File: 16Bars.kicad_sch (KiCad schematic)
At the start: 35 parts, among them IC1 CD4033BE, IC2 CD4033BE, IC3 CD4510BE, J1 CLOCK_IN, J2 Conn_02x05_Odd_Even, Q1 2N3904, Q2 2N3904, Q3 2N3904, Q4 2N3904, Q5 2N3904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

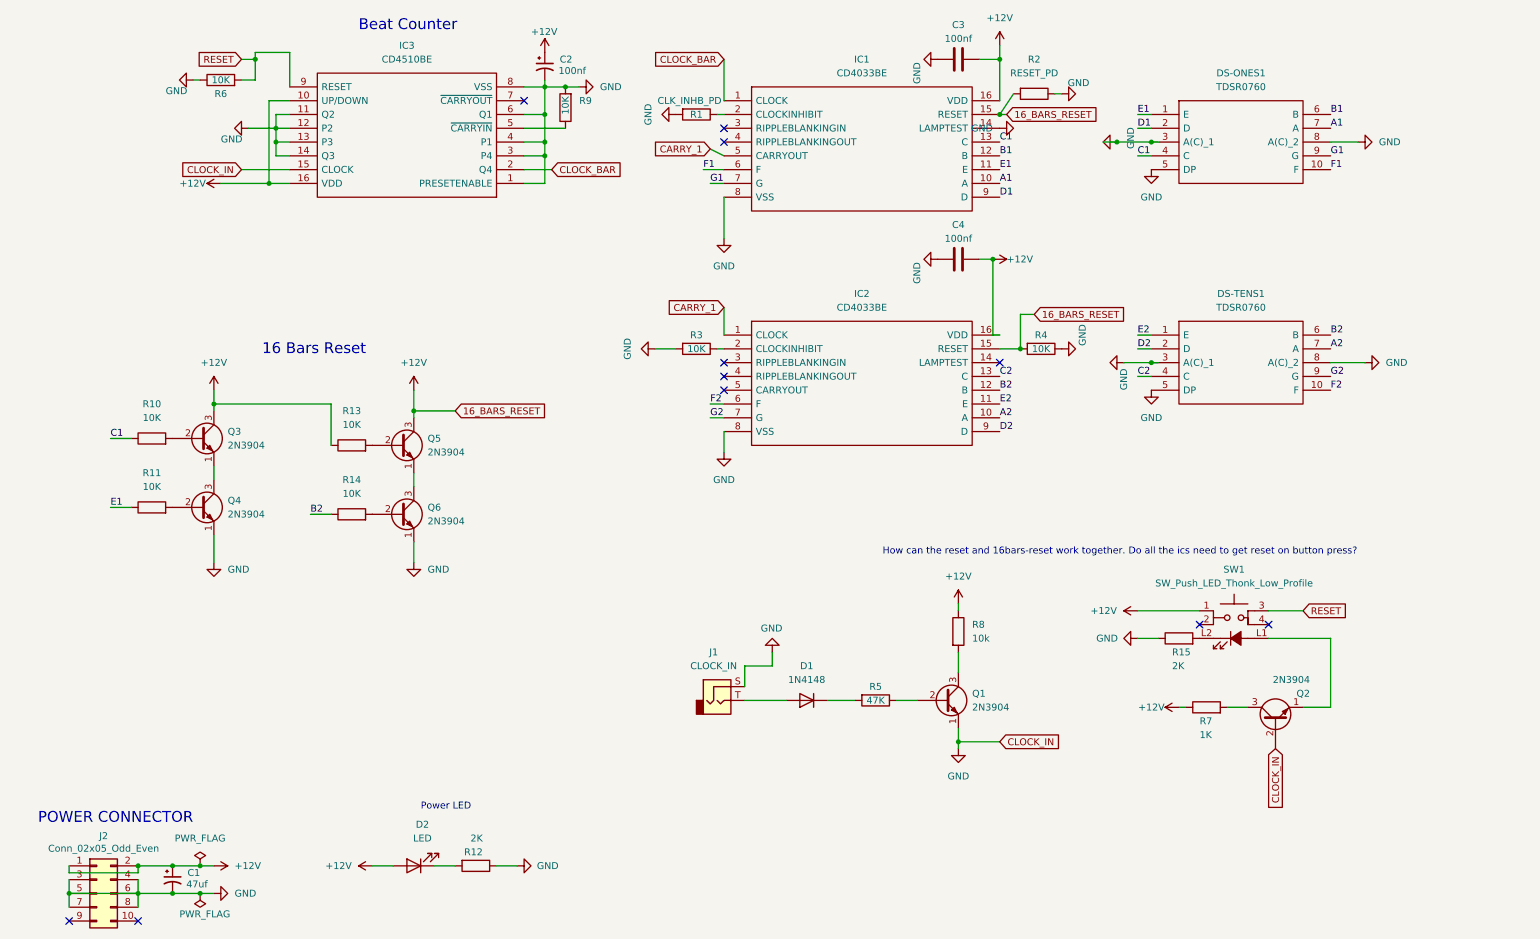
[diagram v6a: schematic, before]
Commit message: Add PowerLED. Add ThonkButton Symbol and Footprint
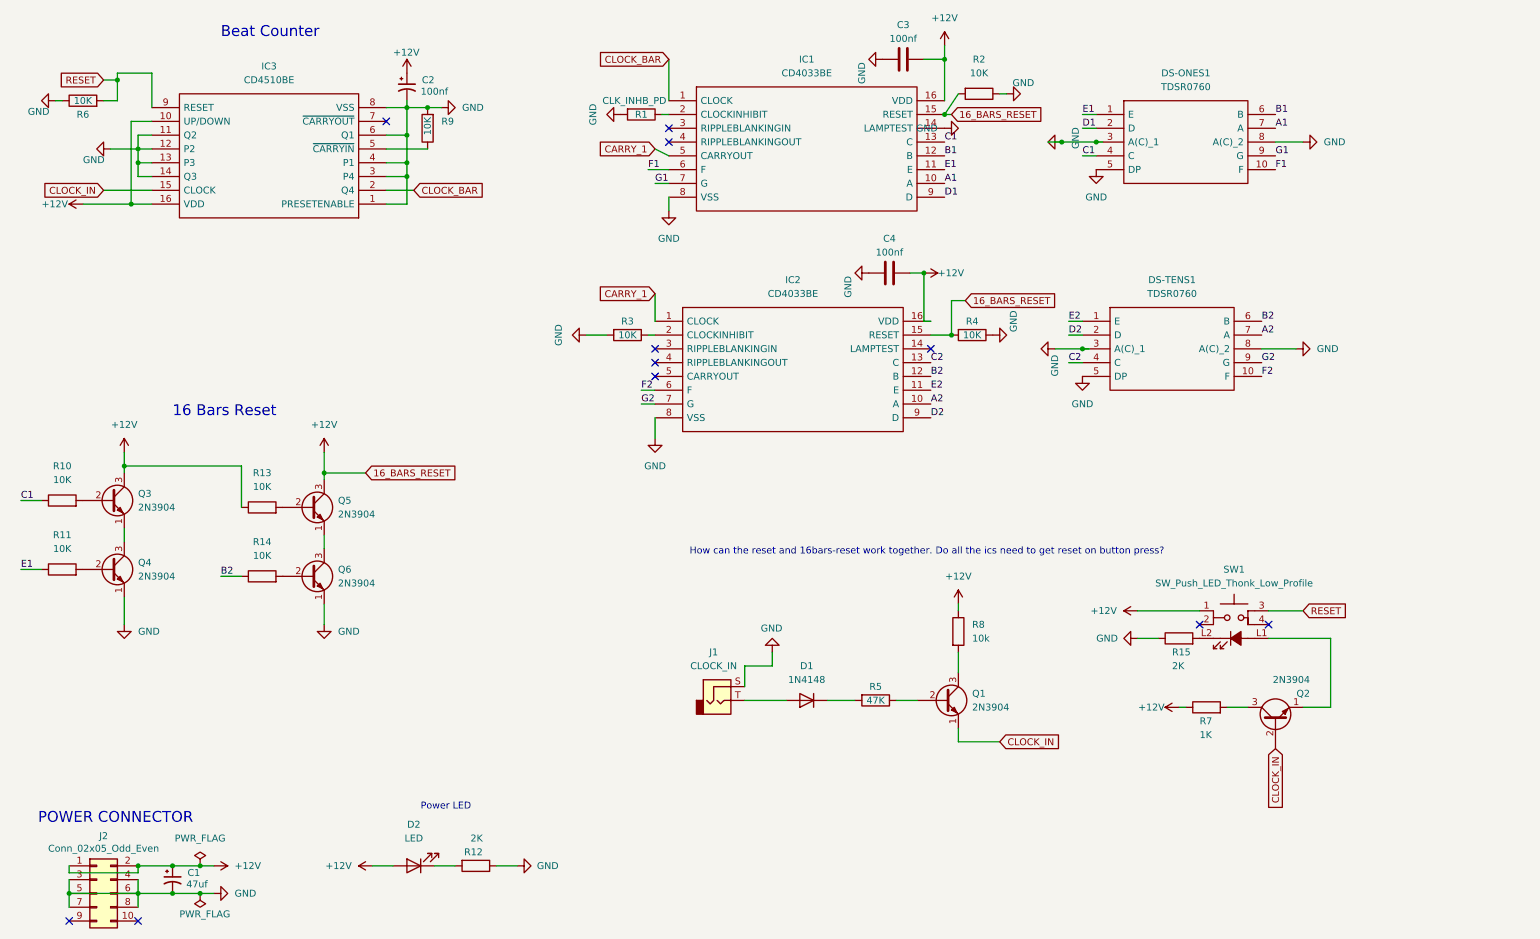
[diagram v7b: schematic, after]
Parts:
- D1: footprint Diode_THT:D_A-405_P7.62mm_Horizontal -> Diode_SMD:D_SOD-323
- D2: footprint (none) -> LED_THT:LED_D3.0mm
- R2: value RESET_PD -> 10K
- SW1: footprint Button_Switch_THT:Thonk-LED-Button-MomentaryON -> TDSR*:ThonkLowProfileButton
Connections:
- net GND: no longer IC3.15 (CLOCK), Q1.1 (E), Q2.2 (B)
- new net CLOCK_IN: IC3.15 (CLOCK), Q1.1 (E), Q2.2 (B)
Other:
- company: 16thWind -> SixteenWinds
- moved on the sheet: C2, C3, C4, DS-ONES1, DS-TENS1, IC1, IC2, IC3, Q3, Q4, Q5, Q6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

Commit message: Complete Surface Mount Version
Fix 16BarsReset Label by adding resistor
Add TODOs for clock and bar division switches
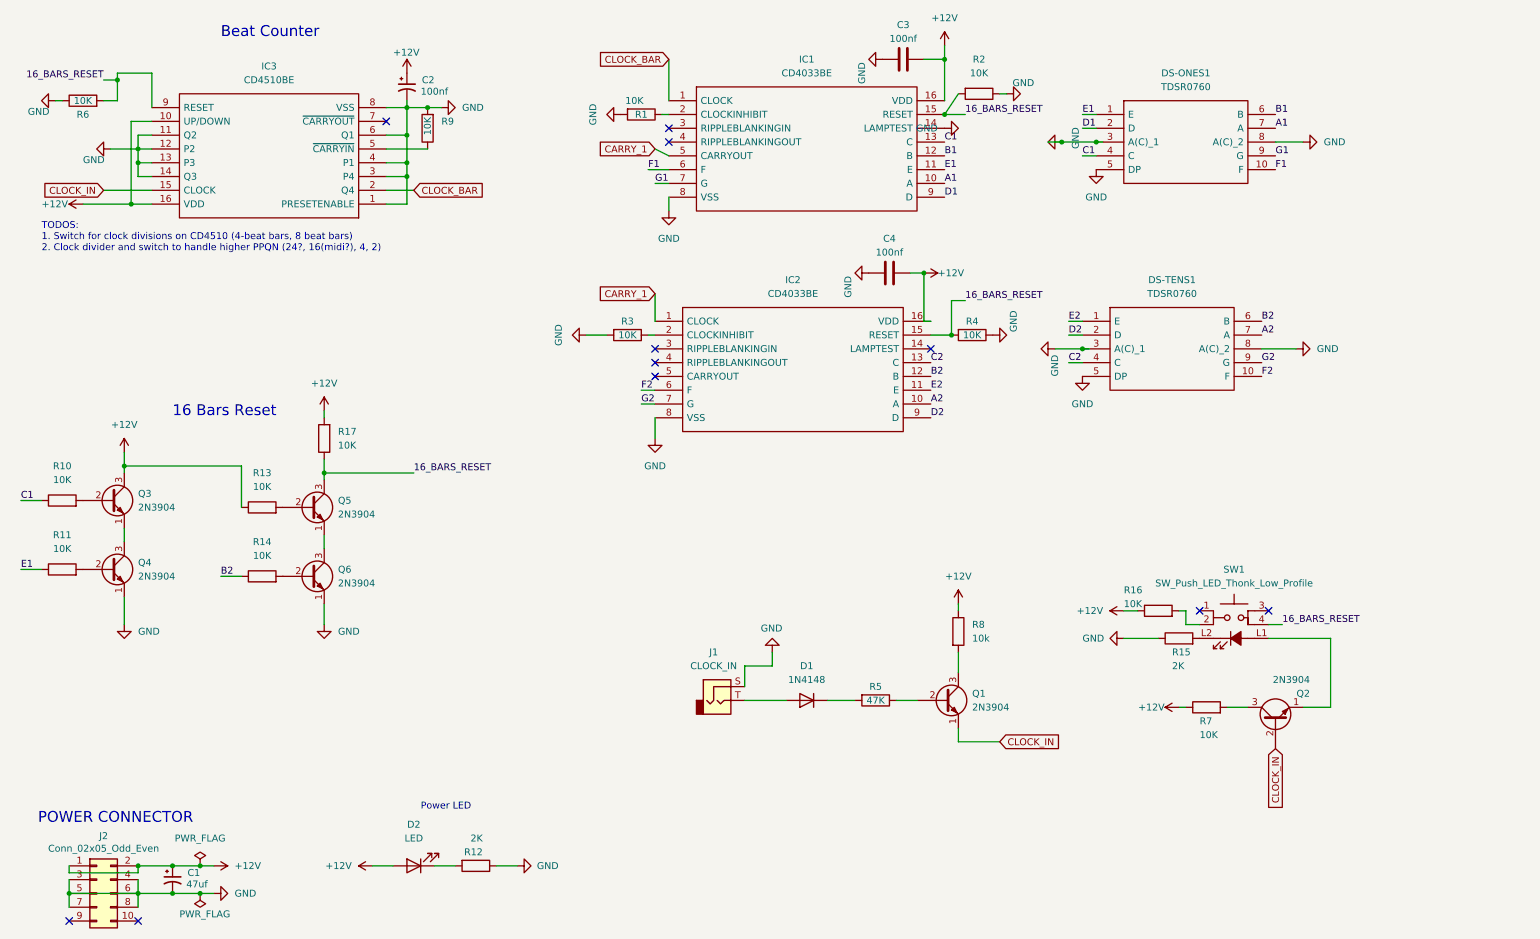
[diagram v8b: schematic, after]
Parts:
- added R16, R17: 10K, Resistor_SMD:R_0402_1005Metric, symbol Device:R
- R1: value CLK_INHB_PD -> 10K
- R7: value 1K -> 10K
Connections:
- net +12V: now also R16.1, R17.2; no longer IC1.15 (RESET), IC2.15 (RESET), Q5.3 (C), R2.2, R4.2, SW1.1
- net at SW1.2: now also R16.2
- net 16_BARS_RESET: now reaches SW1.4
- net 16_BARS_RESET: now also IC1.15 (RESET), IC2.15 (RESET), IC3.9 (RESET), Q5.3 (C), R2.2, R4.2, R6.2, R17.1
- removed net RESET: IC3.9 (RESET), R6.2, SW1.3
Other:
- note added: "TODOS: 1. Switch for clock divisions on CD4510 (4-beat bars, 8 beat bars) 2. Clock divider and switch to handle higher PPQN (24?, 16(midi?), 4, 2)"
- note removed: "How can the reset and 16bars-reset work together. Do all the ics need to get reset on button press?"
